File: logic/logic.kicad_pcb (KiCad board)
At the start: 4 copper layers, 162 x 77.9 mm, 36 parts, among them J1 DIN41612_03x32_ABC, J2 Conn_02x05_Odd_Even, J3 Conn_02x05_Odd_Even, J4 Conn_02x05_Odd_Even, U1 TPIC6595, U14 74HC14, U2 TPIC6595, U3 TPIC6595, U4 TPIC6595, U5 TPIC6595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

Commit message: Ongoing development of logic board.
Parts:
- moved C6 51.2 mm to (113.0, 101.3)
- moved U9 51.2 mm to (102.4, 101.3)
- moved C5 34.1 mm to (122.1, 131.8), turned to 0 degrees
- moved R3 26.6 mm to (99.6, 78.9), turned to -90 degrees
- moved U5 15.4 mm to (128.8, 56.1)
- moved C7 15.4 mm to (125.9, 58.6)
- moved C11 13.1 mm to (126.0, 103.8)
- moved U4 13.1 mm to (128.9, 101.3)
- moved C8 13.0 mm to (143.2, 58.6)
- moved U6 13.0 mm to (146.2, 56.1)
- moved C9 10.6 mm to (160.6, 58.6)
- moved U7 10.6 mm to (163.6, 56.1)
- moved C12 8.91 mm to (140.5, 103.8)
- moved U3 8.91 mm to (143.5, 101.3)
- moved C10 8.37 mm to (178.1, 58.6)
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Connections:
- A1 pad D7: Net-(U9-I0a) -> Net-(U9-I3a)
- RN1 pad 10: Net-(J3-Pin_4) -> Net-(J3-Pin_5)
- RN1 pad 11: Net-(J3-Pin_2) -> Net-(J3-Pin_4)
- RN1 pad 12: Net-(J3-Pin_1) -> Net-(J3-Pin_3)
- RN1 pad 13: Net-(J3-Pin_3) -> Net-(J3-Pin_2)
- RN1 pad 14: Net-(J3-Pin_5) -> Net-(J3-Pin_1)
- U9 pad 2: Net-(U9-I0a) -> /~{SRCLR3.3}
- U9 pad 8: /~{SRCLR3.3} -> Net-(U9-I3a)
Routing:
- net Net-(J3-Pin_2): track 0.00 -> 109.9 mm
- net Net-(J3-Pin_4): track 0.00 -> 108.6 mm
- net Net-(J3-Pin_1): track 0.00 -> 107.5 mm
- net Net-(J3-Pin_6): track 0.00 -> 107.4 mm
- net Net-(J3-Pin_3): track 0.00 -> 106.2 mm
- net Net-(J3-Pin_5): track 0.00 -> 104.8 mm
- net Net-(J2-Pin_9): track 0.00 -> 74.7 mm
- net Net-(J2-Pin_7): track 0.00 -> 72.0 mm
- net Net-(J2-Pin_5): track 0.00 -> 69.3 mm
- net Net-(J2-Pin_3): track 0.00 -> 66.6 mm
- net Net-(J2-Pin_1): track 0.00 -> 64.4 mm
- net /SRCK: track 59.4 -> 0.00 mm
- net /~{SRCLR}: track 59.4 -> 0.00 mm
- net /RCLK: track 59.3 -> 0.00 mm
- net POR: track 96.2 -> 136.7 mm, vias 0 -> 2
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
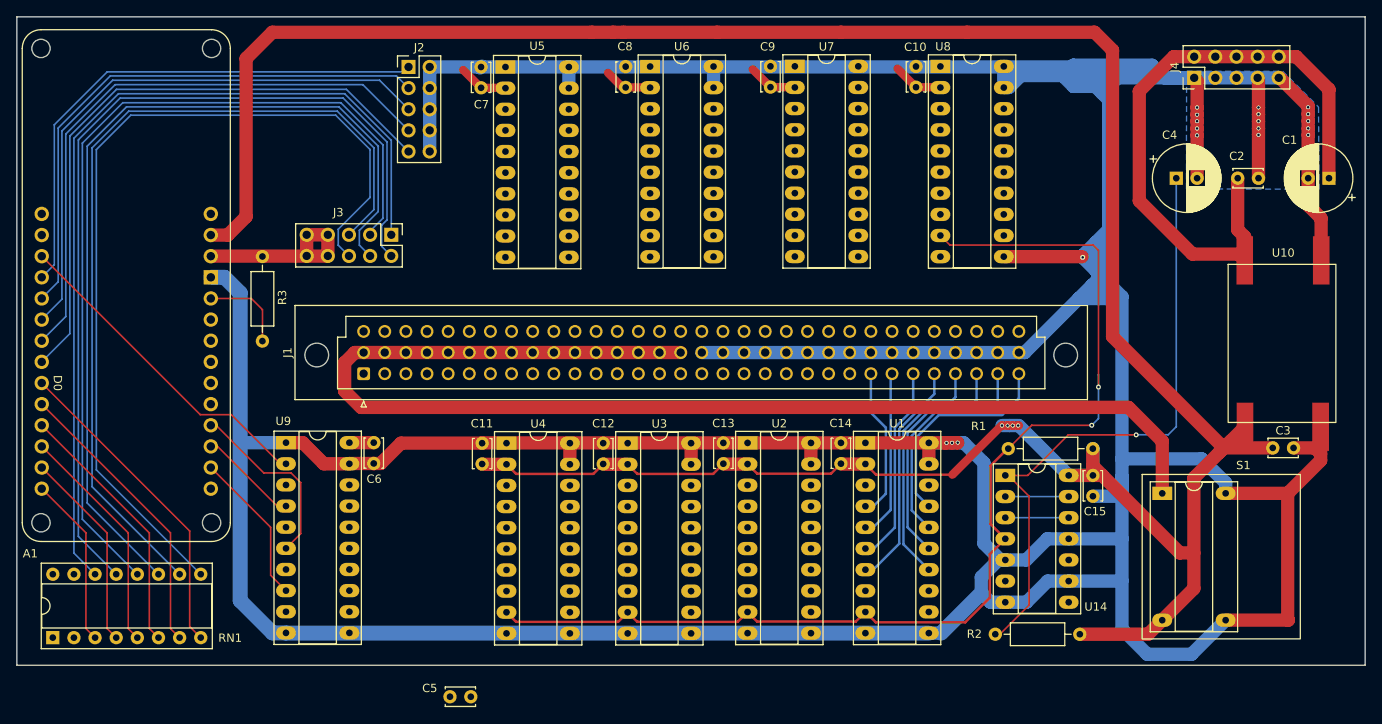
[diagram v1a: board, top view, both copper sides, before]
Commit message: Logic board is mostly routed. Changes to schematic for routing.
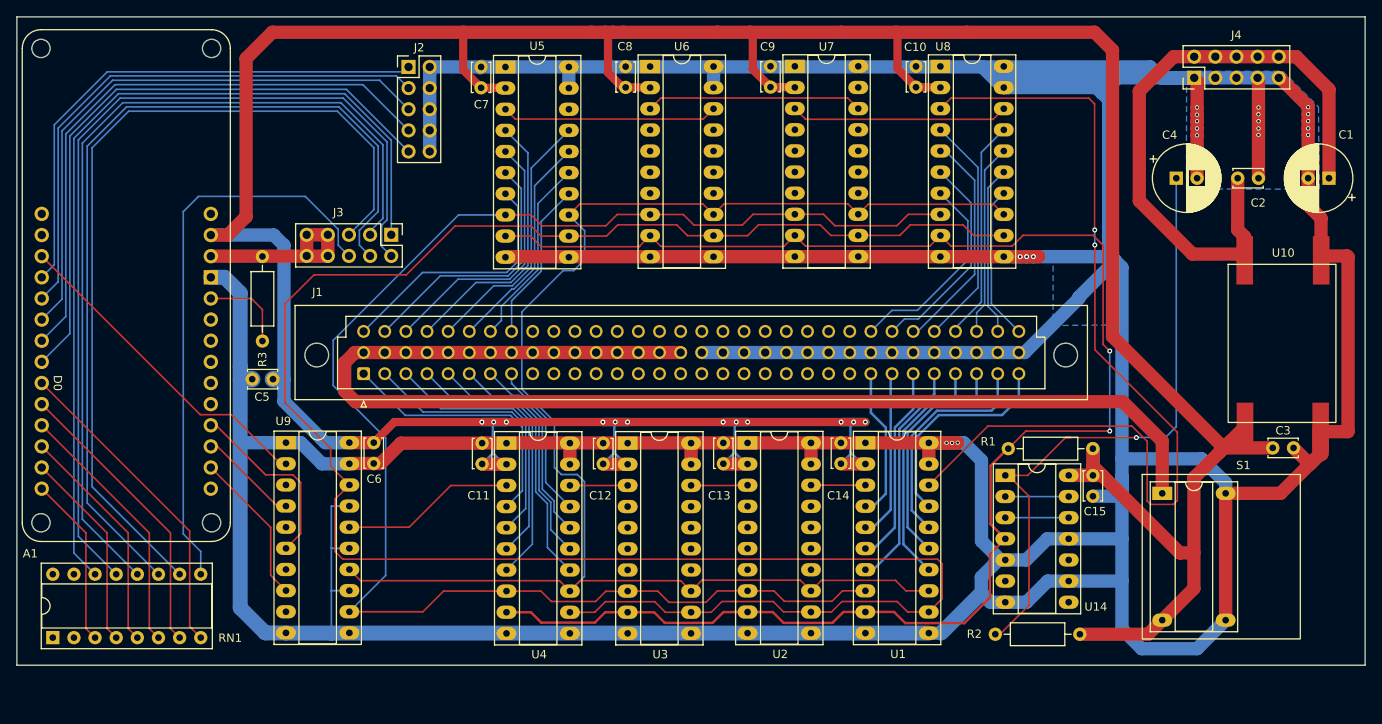
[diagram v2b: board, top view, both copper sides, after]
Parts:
- moved C5 43.7 mm to (100.8, 93.7), turned to 180 degrees
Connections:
- U1 pad 18: Net-(U1-SER_OUT) -> /Sin8
- U1 pad 3: /COPI -> /Sin1
- U2 pad 18: Net-(U2-SER_OUT) -> /Sin1
- U2 pad 3: Net-(U1-SER_OUT) -> /Sin2
- U3 pad 18: Net-(U3-SER_OUT) -> /Sin2
- U3 pad 3: Net-(U2-SER_OUT) -> /Sin3
- U4 pad 18: Net-(U4-SER_OUT) -> /Sin3
- U4 pad 3: Net-(U3-SER_OUT) -> /Sin4
- U5 pad 14: /B5-4 -> /B5-7
- U5 pad 15: /B5-5 -> /B5-6
- U5 pad 16: /B5-6 -> /B5-5
- U5 pad 17: /B5-7 -> /B5-4
- U5 pad 18: Net-(U5-SER_OUT) -> unconnected-(U5-SER_OUT-Pad18)
- U5 pad 3: Net-(U4-SER_OUT) -> /Sin5
- U5 pad 4: /B5-0 -> /B5-3
- U5 pad 5: /B5-1 -> /B5-2
- U5 pad 6: /B5-2 -> /B5-1
- U5 pad 7: /B5-3 -> /B5-0
- U6 pad 14: /B6-4 -> /B6-7
- U6 pad 15: /B6-5 -> /B6-6
- U6 pad 16: /B6-6 -> /B6-5
- U6 pad 17: /B6-7 -> /B6-4
- U6 pad 18: Net-(U6-SER_OUT) -> /Sin5
- U6 pad 3: Net-(U5-SER_OUT) -> /Sin6
- U6 pad 4: /B6-0 -> /B6-3
- U6 pad 5: /B6-1 -> /B6-2
- U6 pad 6: /B6-2 -> /B6-1
- U6 pad 7: /B6-3 -> /B6-0
- U7 pad 14: /B7-4 -> /B7-7
- U7 pad 15: /B7-5 -> /B7-6
- U7 pad 16: /B7-6 -> /B7-5
- U7 pad 17: /B7-7 -> /B7-4
- U7 pad 18: Net-(U7-SER_OUT) -> /Sin6
- U7 pad 3: Net-(U6-SER_OUT) -> /Sin7
- U7 pad 4: /B7-0 -> /B7-3
- U7 pad 5: /B7-1 -> /B7-2
- U7 pad 6: /B7-2 -> /B7-1
- U7 pad 7: /B7-3 -> /B7-0
- U8 pad 14: /B8-4 -> /B8-7
- U8 pad 15: /B8-5 -> /B8-6
- U8 pad 16: /B8-6 -> /B8-5
- U8 pad 17: /B8-7 -> /B8-4
- U8 pad 18: unconnected-(U8-SER_OUT-Pad18) -> /Sin7
- U8 pad 3: Net-(U7-SER_OUT) -> /Sin8
- U8 pad 4: /B8-0 -> /B8-3
- U8 pad 5: /B8-1 -> /B8-2
- U8 pad 6: /B8-2 -> /B8-1
- U8 pad 7: /B8-3 -> /B8-0
- U9 pad 16: /COPI -> /Sin4
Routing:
- net /RCLK: track 0.00 -> 254.6 mm
- net /~{SRCLR}: track 0.00 -> 185.8 mm
- net /SRCK: track 0.00 -> 184.1 mm
- net /Sin8: track 0.00 -> 112.4 mm, vias 0 -> 2
- net GND: track 725.8 -> 835.9 mm, vias 19 -> 21
- net V5.0: track 374.4 -> 477.4 mm, vias 4 -> 12
- net POR: track 136.7 -> 195.6 mm
- net Net-(J3-Pin_6): track 107.4 -> 69.2 mm
- net /B4-3: track 0.00 -> 34.1 mm
- net /B4-2: track 0.00 -> 33.4 mm
- net /B5-3: track 0.00 -> 32.8 mm
- net /B4-1: track 0.00 -> 32.7 mm
- net /B4-4: track 0.00 -> 32.4 mm
- net /B5-2: track 0.00 -> 32.1 mm
- net /B4-0: track 0.00 -> 32.1 mm
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
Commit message: Routing is complete. Validation and checking begins.
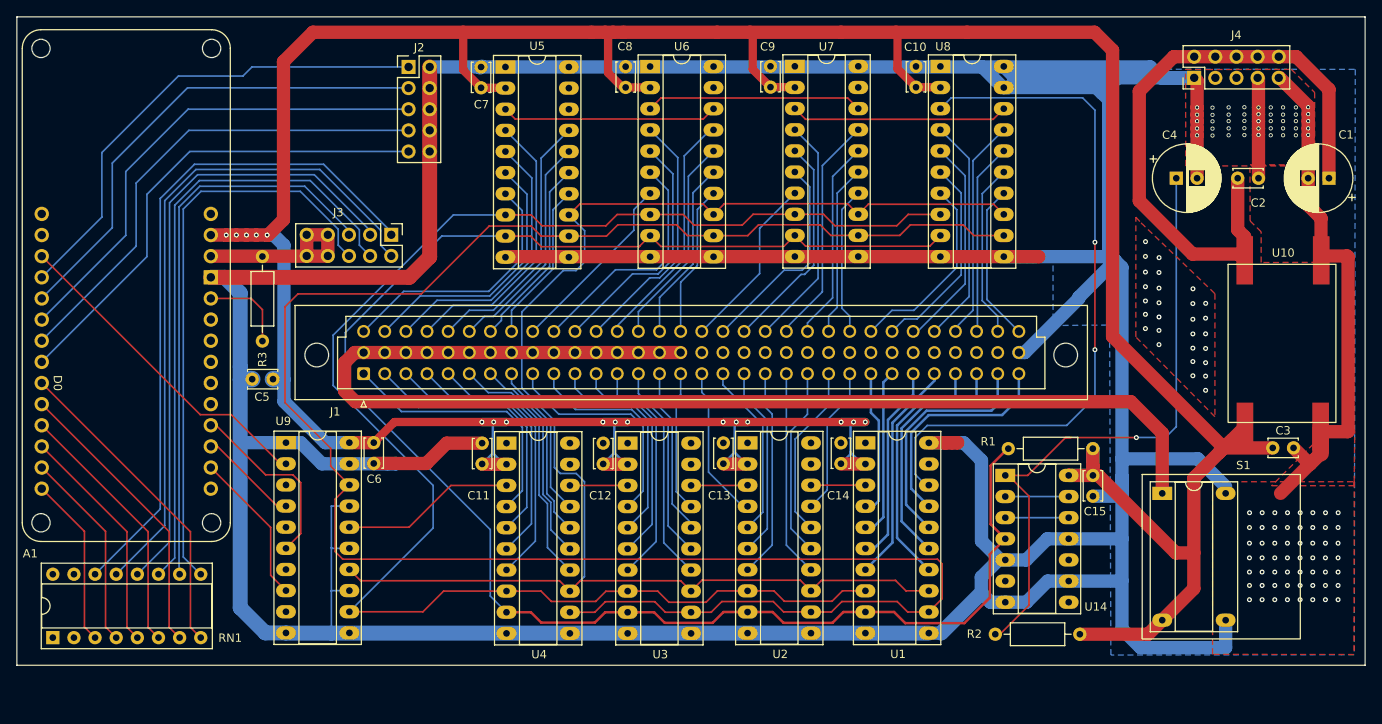
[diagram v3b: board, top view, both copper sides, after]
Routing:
- net GND: track 835.9 -> 1165.3 mm, vias 21 -> 129
- net Net-(J3-Pin_5): track 104.8 -> 68.3 mm
- net Net-(J3-Pin_4): track 108.6 -> 74.7 mm
- net Net-(J3-Pin_3): track 106.2 -> 75.0 mm
- net /B6-3: track 0.00 -> 30.4 mm
- net /B3-3: track 0.00 -> 29.8 mm
- net /B6-2: track 0.00 -> 29.5 mm
- net /B6-4: track 0.00 -> 29.2 mm
- net /B3-2: track 0.00 -> 29.0 mm
- net /B7-4: track 0.00 -> 28.9 mm
- net /B6-1: track 0.00 -> 28.6 mm
- net /B3-4: track 0.00 -> 28.5 mm
- net Net-(J3-Pin_2): track 109.9 -> 81.4 mm
- net /B3-1: track 0.00 -> 28.1 mm
- net /B7-3: track 0.00 -> 28.0 mm
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- added copper zone on F.Cu, net GND
- added copper zone on In1.Cu, net GND
- added copper zone on In2.Cu, net GND

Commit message: DRC warnings evaluated
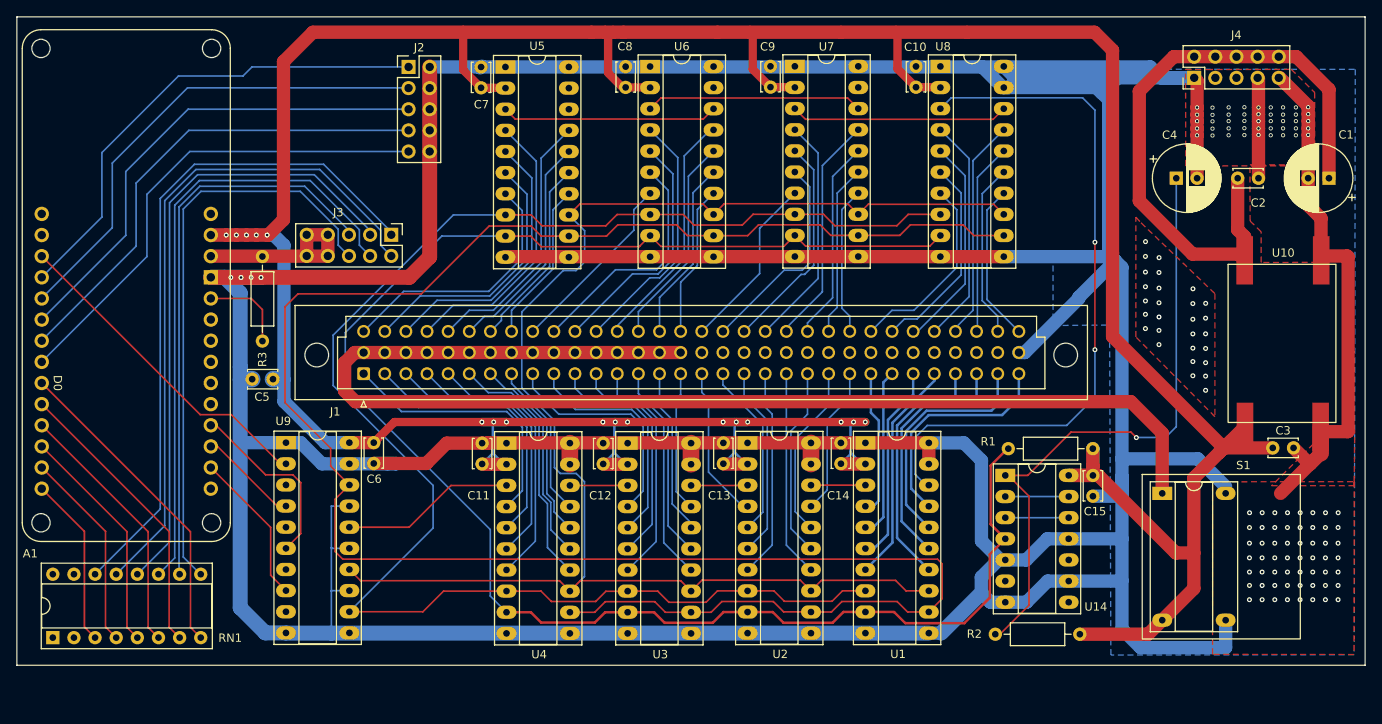
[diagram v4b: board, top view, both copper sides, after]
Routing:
- net GND: track 1165.3 -> 1227.9 mm, vias 129 -> 133
- net V5.0: track 475.8 -> 478.4 mm

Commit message: Minor fussing and run DRC. Generate Gerbers and drill files.
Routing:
- net GND: track 1227.9 -> 1278.0 mm, vias 133 -> 140
